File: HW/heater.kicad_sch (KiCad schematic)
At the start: 13 parts, among them J1 Heater, Q1 RQ3E110AJ

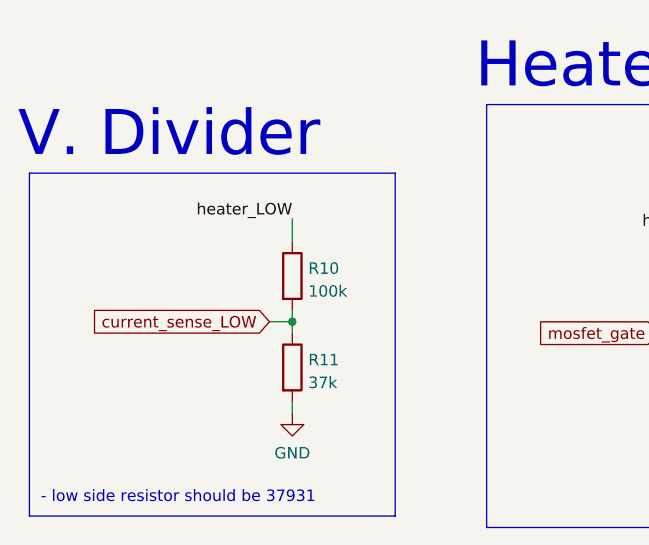
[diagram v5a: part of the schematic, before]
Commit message: Fix board, QOL fixes
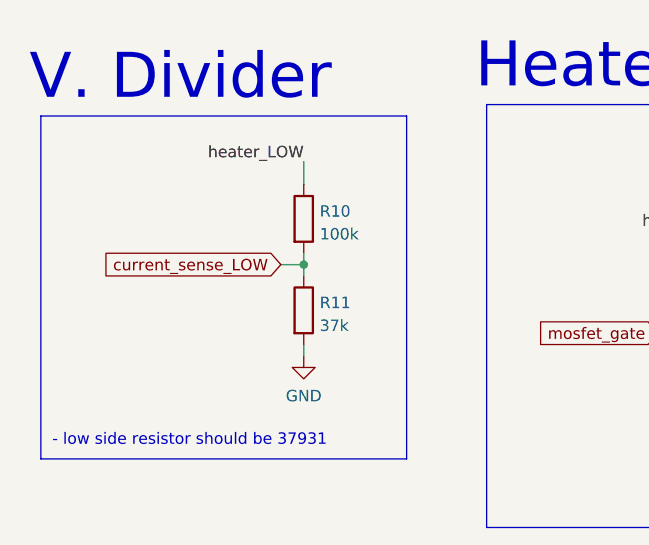
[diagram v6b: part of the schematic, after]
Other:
- moved on the sheet: R10, R11
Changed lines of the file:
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@@
   (junction (at 208.28 86.36) (diameter 0) (color 0 0 0 0)
   )
-  (junction (at 91.44 101.6) (diameter 0) (color 0 0 0 0)
+  (junction (at 92.71 95.25) (diameter 0) (color 0 0 0 0)
   )
   (junction (at 226.06 111.76) (diameter 0) (color 0 0 0 0)
@@
     (stroke (width 0) (type default) (color 0 0 0 0))
   )
-  (wire (pts (xy 88.9 101.6) (xy 91.44 101.6))
+  (wire (pts (xy 90.17 95.25) (xy 92.71 95.25))
     (stroke (width 0) (type default) (color 0 0 0 0))
   )
@@
     (stroke (width 0) (type default) (color 0 0 0 0))
   )
-  (wire (pts (xy 91.44 90.17) (xy 91.44 92.71))
-    (stroke (width 0) (type default) (color 0 0 0 0))
-  )
-  (wire (pts (xy 91.44 101.6) (xy 91.44 102.87))
+  (wire (pts (xy 92.71 83.82) (xy 92.71 86.36))
+    (stroke (width 0) (type default) (color 0 0 0 0))
+  )
+  (wire (pts (xy 92.71 95.25) (xy 92.71 96.52))
     (stroke (width 0) (type default) (color 0 0 0 0))
   )
@@
     (stroke (width 0) (type default) (color 0 0 0 0))
   )
-  (polyline (pts (xy 62.23 85.09) (xy 62.23 123.19))
+  (polyline (pts (xy 63.5 78.74) (xy 63.5 116.84))
     (stroke (width 0) (type default) (color 0 0 0 0))
   )
@@
     (stroke (width 0) (type default) (color 0 0 0 0))
   )
-  (polyline (pts (xy 62.23 123.19) (xy 102.87 123.19))
-    (stroke (width 0) (type default) (color 0 0 0 0))
-  )
-  (polyline (pts (xy 62.23 85.09) (xy 102.87 85.09))
+  (polyline (pts (xy 63.5 116.84) (xy 104.14 116.84))
+    (stroke (width 0) (type default) (color 0 0 0 0))
+  )
+  (polyline (pts (xy 63.5 78.74) (xy 104.14 78.74))
     (stroke (width 0) (type default) (color 0 0 0 0))
   )
@@
     (stroke (width 0) (type default) (color 0 0 0 0))
   )
-  (polyline (pts (xy 102.87 123.19) (xy 102.87 85.09))
+  (polyline (pts (xy 104.14 116.84) (xy 104.14 78.74))
     (stroke (width 0) (type default) (color 0 0 0 0))
   )
@@
     (stroke (width 0) (type default) (color 0 0 0 0))
   )
-  (wire (pts (xy 91.44 110.49) (xy 91.44 111.76))
+  (wire (pts (xy 92.71 104.14) (xy 92.71 105.41))
     (stroke (width 0) (type default) (color 0 0 0 0))
   )
@@
     (stroke (width 0) (type default) (color 0 0 0 0))
   )
-  (wire (pts (xy 91.44 100.33) (xy 91.44 101.6))
+  (wire (pts (xy 92.71 93.98) (xy 92.71 95.25))
     (stroke (width 0) (type default) (color 0 0 0 0))
   )
@@
     (stroke (width 0) (type default) (color 0 0 0 0))
   )
-  (text "V. Divider" (at 60.96 83.82 0)
+  (text "V. Divider" (at 62.23 77.47 0)
     (effects (font (size 5 5)) (justify left bottom))
   )
@@
     (effects (font (size 5 5)) (justify left bottom))
   )
-  (text "- low side resistor should be 37931" (at 63.5 121.92 0)
+  (text "- low side resistor should be 37931" (at 64.77 115.57 0)
     (effects (font (size 1.27 1.27)) (justify left bottom))
   )
@@
     (effects (font (size 1.27 1.27)) (justify right bottom))
   )
-  (label "heater_LOW" (at 91.44 90.17 180)
+  (label "heater_LOW" (at 92.71 83.82 180)
     (effects (font (size 1.27 1.27)) (justify right bottom))
   )
@@
     )
   )
-  (global_label "current_sense_LOW" (shape input) (at 88.9 101.6 180) (fields_autoplaced)
-    (effects (font (size 1.27 1.27)) (justify right))
-    (property "Intersheet References" "${INTERSHEET_REFS}" (id 0) (at 68.5859 101.6794 0)
+  (global_label "current_sense_LOW" (shape input) (at 90.17 95.25 180) (fields_autoplaced)
+    (effects (font (size 1.27 1.27)) (justify right))
+    (property "Intersheet References" "${INTERSHEET_REFS}" (id 0) (at 69.8559 95.3294 0)
       (effects (font (size 1.27 1.27)) (justify right) hide)
     )
@@
     (pin "2")
   )
-  (symbol (lib_id "power:GND") (at 91.44 111.76 0) (unit 1)
-    (in_bom yes) (on_board yes) (fields_autoplaced)
-    (property "Reference" "#PWR0115" (id 0) (at 91.44 118.11 0)
-      (effects (font (size 1.27 1.27)) hide)
-    )
-    (property "Value" "GND" (id 1) (at 91.44 116.2034 0))
-    (property "Footprint" "" (id 2) (at 91.44 111.76 0)
-      (effects (font (size 1.27 1.27)) hide)
-    )
-    (property "Datasheet" "" (id 3) (at 91.44 111.76 0)
+  (symbol (lib_id "power:GND") (at 92.71 105.41 0) (unit 1)
+    (in_bom yes) (on_board yes) (fields_autoplaced)
+    (property "Reference" "#PWR0115" (id 0) (at 92.71 111.76 0)
+      (effects (font (size 1.27 1.27)) hide)
+    )
+    (property "Value" "GND" (id 1) (at 92.71 109.8534 0))
+    (property "Footprint" "" (id 2) (at 92.71 105.41 0)
+      (effects (font (size 1.27 1.27)) hide)
+    )
+    (property "Datasheet" "" (id 3) (at 92.71 105.41 0)
       (effects (font (size 1.27 1.27)) hide)
     )
@@
     (pin "1")
   )
-  (symbol (lib_id "Device:R") (at 91.44 106.68 0) (unit 1)
-    (in_bom yes) (on_board yes) (fields_autoplaced)
-    (property "Reference" "R11" (id 0) (at 93.218 105.8453 0)
-      (effects (font (size 1.27 1.27)) (justify left))
-    )
-    (property "Value" "37k" (id 1) (at 93.218 108.3822 0)
-      (effects (font (size 1.27 1.27)) (justify left))
-    )
-    (property "Footprint" "Resistor_SMD:R_0603_1608Metric" (id 2) (at 89.662 106.68 90)
-      (effects (font (size 1.27 1.27)) hide)
-    )
-    (property "Datasheet" "~" (id 3) (at 91.44 106.68 0)
-      (effects (font (size 1.27 1.27)) hide)
-    )
-    (pin "1")
-    (pin "2")
-  )
-  (symbol (lib_id "Device:R") (at 91.44 96.52 0) (unit 1)
-    (in_bom yes) (on_board yes) (fields_autoplaced)
-    (property "Reference" "R10" (id 0) (at 93.218 95.6853 0)
-      (effects (font (size 1.27 1.27)) (justify left))
-    )
-    (property "Value" "100k" (id 1) (at 93.218 98.2222 0)
-      (effects (font (size 1.27 1.27)) (justify left))
-    )
-    (property "Footprint" "Resistor_SMD:R_0603_1608Metric" (id 2) (at 89.662 96.52 90)
-      (effects (font (size 1.27 1.27)) hide)
-    )
-    (property "Datasheet" "~" (id 3) (at 91.44 96.52 0)
-      (effects (font (size 1.27 1.27)) hide)
-    )
+  (symbol (lib_id "Device:R") (at 92.71 100.33 0) (unit 1)
+    (in_bom yes) (on_board yes) (fields_autoplaced)
+    (property "Reference" "R11" (id 0) (at 94.488 99.4953 0)
+      (effects (font (size 1.27 1.27)) (justify left))
+    )
+    (property "Value" "37k" (id 1) (at 94.488 102.0322 0)
+      (effects (font (size 1.27 1.27)) (justify left))
+    )
+    (property "Footprint" "Resistor_SMD:R_0603_1608Metric" (id 2) (at 90.932 100.33 90)
+      (effects (font (size 1.27 1.27)) hide)
+    )
+    (property "Datasheet" "~" (id 3) (at 92.71 100.33 0)
+      (effects (font (size 1.27 1.27)) hide)
+    )
+    (pin "1")
+    (pin "2")
+  )
+  (symbol (lib_id "Device:R") (at 92.71 90.17 0) (unit 1)
+    (in_bom yes) (on_board yes) (fields_autoplaced)
+    (property "Reference" "R10" (id 0) (at 94.488 89.3353 0)
+      (effects (font (size 1.27 1.27)) (justify left))
+    )
+    (property "Value" "100k" (id 1) (at 94.488 91.8722 0)
+      (effects (font (size 1.27 1.27)) (justify left))
+    )
+    (property "Footprint" "Resistor_SMD:R_0603_1608Metric" (id 2) (at 90.932 90.17 90)
+      (effects (font (size 1.27 1.27)) hide)
+    )
+    (property "Datasheet" "~" (id 3) (at 92.71 90.17 0)
+      (effects (font (size 1.27 1.27)) hide)
+    )

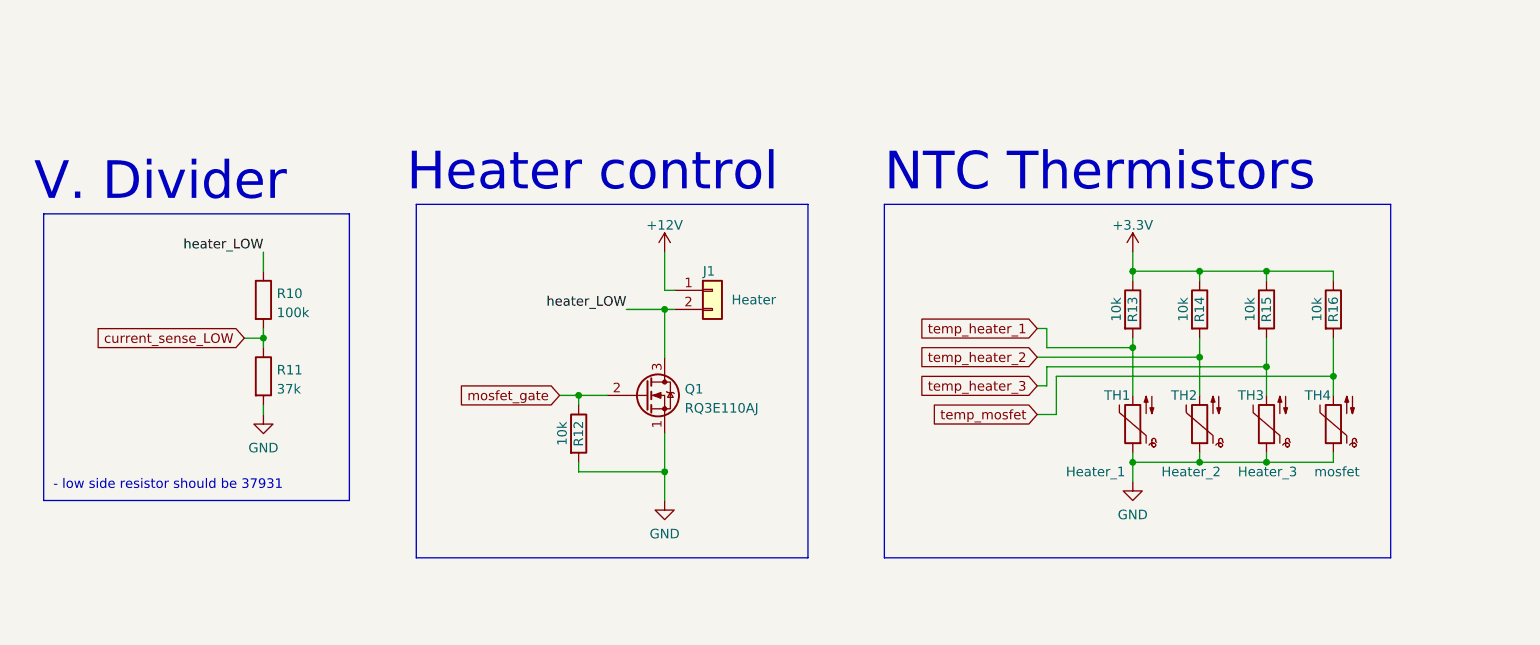
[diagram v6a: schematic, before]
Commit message: QOL changes on pcb, fixed wrong ACDC brick polarity xD
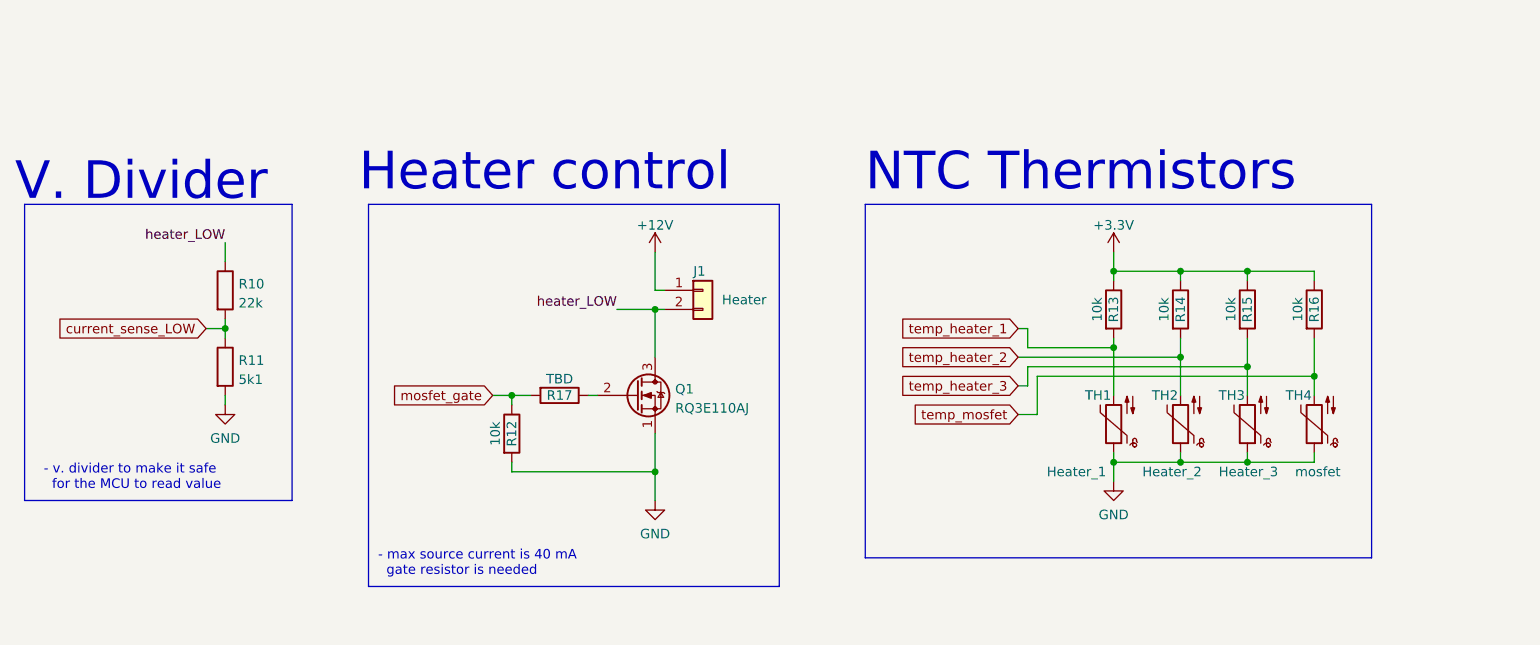
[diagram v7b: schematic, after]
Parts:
- added R17: TBD, Resistor_SMD:R_0603_1608Metric, symbol Device:R
- R10: value 100k -> 22k
- R11: value 37k -> 5k1
- TH1, TH2, TH3, TH4: footprint TestPoint:TestPoint_2Pads_Pitch2.54mm_Drill0.8mm -> Jumper:SolderJumper-2_P1.3mm_Open_RoundedPad1.0x1.5mm
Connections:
- net mosfet_gate: now also R17.2; no longer Q1.2 (G)
- new net: Q1.2 (G), R17.1
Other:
- note added: "- max source current is 40 mA gate resistor is needed"
- note added: "- v. divider to make it safe for the MCU to read value"
- note removed: "- low side resistor should be 37931"
- moved on the sheet: J1, Q1, R10, R11, R12, R13, R14, R15, R16, TH1, TH2, TH3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

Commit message: revision 0
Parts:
- R17: value TBD -> 0
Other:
- note removed: "- max source current is 40 mA gate resistor is needed"
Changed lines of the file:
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@@
     (stroke (width 0) (type default) (color 0 0 0 0))
   )
-  (wire (pts (xy 139.7 91.44) (xy 144.78 91.44))
+  (wire (pts (xy 132.08 91.44) (xy 144.78 91.44))
     (stroke (width 0) (type default) (color 0 0 0 0))
   )
@@
     (stroke (width 0) (type default) (color 0 0 0 0))
   )
-  (polyline (pts (xy 161.29 128.27) (xy 161.29 77.47))
+  (polyline (pts (xy 161.29 123.19) (xy 161.29 77.47))
     (stroke (width 0) (type default) (color 0 0 0 0))
   )
@@
     (stroke (width 0) (type default) (color 0 0 0 0))
   )
-  (polyline (pts (xy 106.68 128.27) (xy 161.29 128.27))
+  (polyline (pts (xy 106.68 123.19) (xy 161.29 123.19))
     (stroke (width 0) (type default) (color 0 0 0 0))
   )
@@
     (stroke (width 0) (type default) (color 0 0 0 0))
   )
-  (polyline (pts (xy 106.68 77.47) (xy 106.68 128.27))
+  (polyline (pts (xy 106.68 77.47) (xy 106.68 123.19))
     (stroke (width 0) (type default) (color 0 0 0 0))
   )
@@
     (effects (font (size 5 5)) (justify left bottom))
   )
-  (text "- max source current is 40 mA\n  gate resistor is needed"
-    (at 107.95 127 0)
+  (label "heater_LOW" (at 132.08 91.44 0)
     (effects (font (size 1.27 1.27)) (justify left bottom))
-  )
-  (label "heater_LOW" (at 139.7 91.44 180)
-    (effects (font (size 1.27 1.27)) (justify right bottom))
   )
   (label "heater_LOW" (at 87.63 82.55 180)
@@
     (in_bom yes) (on_board yes)
     (property "Reference" "R17" (id 0) (at 132.08 102.87 90))
-    (property "Value" "TBD" (id 1) (at 132.08 100.6911 90))
+    (property "Value" "0" (id 1) (at 132.08 100.6911 90))
     (property "Footprint" "Resistor_SMD:R_0603_1608Metric" (id 2) (at 132.08 101.092 90)
       (effects (font (size 1.27 1.27)) hide)
